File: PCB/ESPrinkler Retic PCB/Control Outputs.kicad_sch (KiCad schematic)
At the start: 108 parts, among them Q1 Q_NMOS, Q10 Q_NMOS, Q11 Q_NMOS, Q4 Q_NMOS, Q5 Q_NMOS, Q6 Q_NMOS, Q7 Q_NMOS, Q8 Q_NMOS, Q9 Q_NMOS, U1 MOC3063S, U10 MOC3063S, U3 MOC3063S, U4 MOC3063S, U5 MOC3063S, U6 MOC3063S, U7 MOC3063S, U8 MOC3063S, U9 MOC3063S

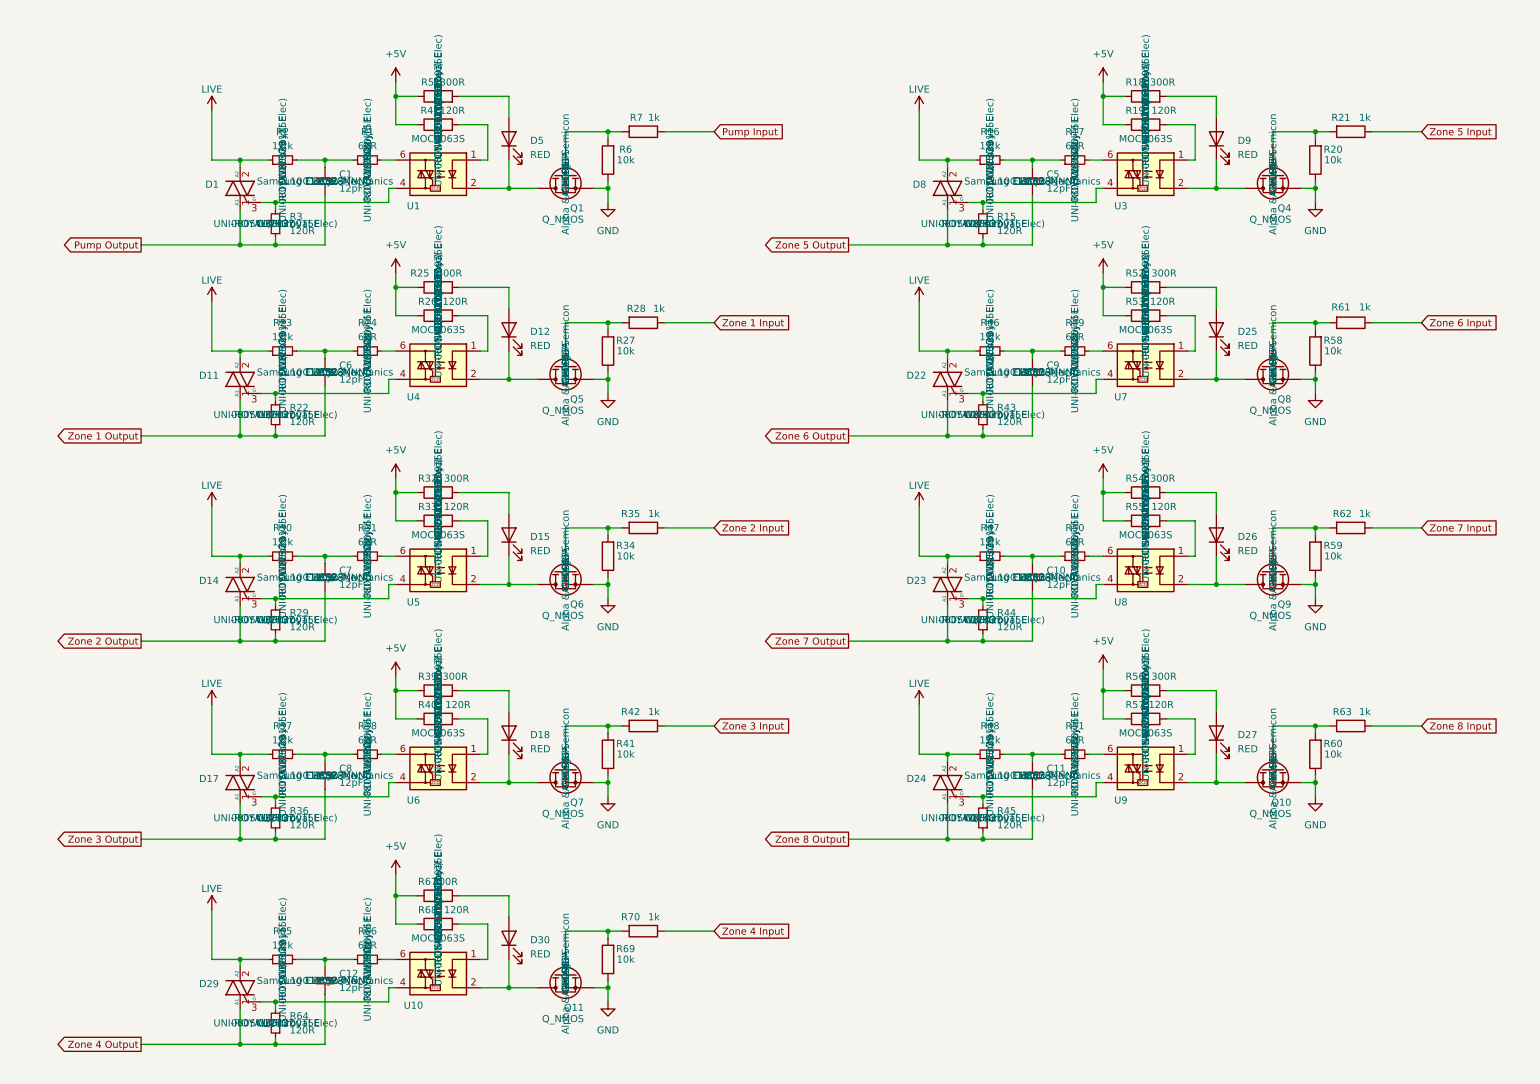
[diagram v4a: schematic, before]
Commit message: Initial schematic design completed
Finish initial schematic design and source all required components. DRC completed with only minor warnings (regarding net names, no worries). Move on to begin PCB design
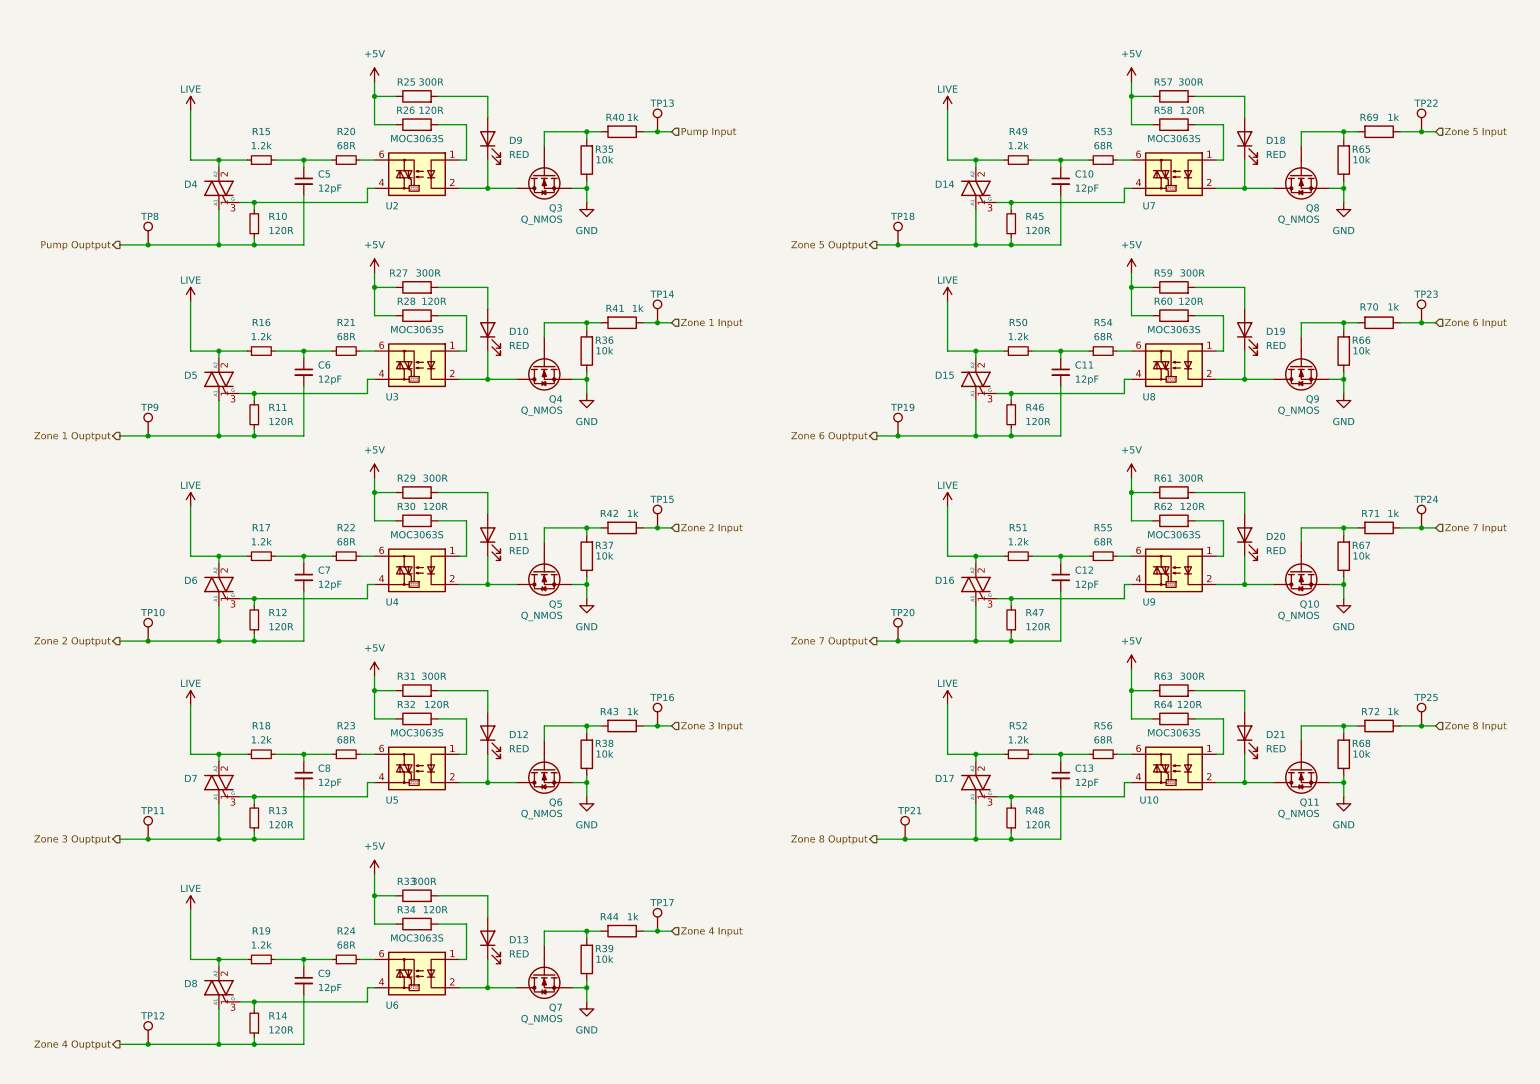
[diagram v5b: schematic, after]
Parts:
- added TP10, TP11, TP12, TP13, TP14, TP15, TP16, TP17, TP18, TP19, TP20, TP21, TP22, TP23, TP24, TP25, TP8, TP9: TestPoint, TestPoint:TestPoint_Pad_D1.5mm, symbol Connector:TestPoint
- D14: renamed from D8; footprint (none) -> Package_TO_SOT_THT:TO-220-3_Horizontal_TabDown; Manufacturer (none) -> STMicroelectronics; Manufacturer P/N (none) -> BTB16-600BWRG; Supplier (none) -> LCSC; Supplier P/N (none) -> C669873
- D15: renamed from D22; footprint (none) -> Package_TO_SOT_THT:TO-220-3_Horizontal_TabDown; Manufacturer (none) -> STMicroelectronics; Manufacturer P/N (none) -> BTB16-600BWRG; Supplier (none) -> LCSC; Supplier P/N (none) -> C669873
- D16: renamed from D23; footprint (none) -> Package_TO_SOT_THT:TO-220-3_Horizontal_TabDown; Manufacturer (none) -> STMicroelectronics; Manufacturer P/N (none) -> BTB16-600BWRG; Supplier (none) -> LCSC; Supplier P/N (none) -> C669873
- D17: renamed from D24; footprint (none) -> Package_TO_SOT_THT:TO-220-3_Horizontal_TabDown; Manufacturer (none) -> STMicroelectronics; Manufacturer P/N (none) -> BTB16-600BWRG; Supplier (none) -> LCSC; Supplier P/N (none) -> C669873
- D4: renamed from D1; footprint (none) -> Package_TO_SOT_THT:TO-220-3_Horizontal_TabDown; Manufacturer (none) -> STMicroelectronics; Manufacturer P/N (none) -> BTB16-600BWRG; Supplier (none) -> LCSC; Supplier P/N (none) -> C669873
- D5: renamed from D11; footprint (none) -> Package_TO_SOT_THT:TO-220-3_Horizontal_TabDown; Manufacturer (none) -> STMicroelectronics; Manufacturer P/N (none) -> BTB16-600BWRG; Supplier (none) -> LCSC; Supplier P/N (none) -> C669873
- D6: renamed from D14; footprint (none) -> Package_TO_SOT_THT:TO-220-3_Horizontal_TabDown; Manufacturer (none) -> STMicroelectronics; Manufacturer P/N (none) -> BTB16-600BWRG; Supplier (none) -> LCSC; Supplier P/N (none) -> C669873
- D7: renamed from D17; footprint (none) -> Package_TO_SOT_THT:TO-220-3_Horizontal_TabDown; Manufacturer (none) -> STMicroelectronics; Manufacturer P/N (none) -> BTB16-600BWRG; Supplier (none) -> LCSC; Supplier P/N (none) -> C669873
- D8: renamed from D29; footprint (none) -> Package_TO_SOT_THT:TO-220-3_Horizontal_TabDown; Manufacturer (none) -> STMicroelectronics; Manufacturer P/N (none) -> BTB16-600BWRG; Supplier (none) -> LCSC; Supplier P/N (none) -> C669873
- renumbered C5 to C10, C9 to C11, C10 to C12, C11 to C13, C1 to C5, C12 to C9, D12 to D10, D15 to D11, D18 to D12, D30 to D13, D9 to D18, D25 to D19, D26 to D20, D27 to D21, D5 to D9, Q9 to Q10, Q10 to Q11, Q1 to Q3, Q5 to Q4, Q6 to Q5, Q7 to Q6, Q11 to Q7, Q4 to Q8, Q8 to Q9, R3 to R10, R22 to R11, R29 to R12, R36 to R13, R64 to R14, R2 to R15, R23 to R16, R30 to R17, R37 to R18, R65 to R19, R1 to R20, R24 to R21, R31 to R22, R38 to R23, R66 to R24, R5 to R25, R4 to R26, R25 to R27, R26 to R28, R32 to R29, R33 to R30, R39 to R31, R40 to R32, R67 to R33, R68 to R34, R6 to R35, R27 to R36, R34 to R37, R41 to R38, R69 to R39, R7 to R40, R28 to R41, R35 to R42, R42 to R43, R70 to R44, R15 to R45, R43 to R46, R44 to R47, R45 to R48, R16 to R49, R46 to R50, R47 to R51, R48 to R52, R17 to R53, R49 to R54, R50 to R55, R51 to R56, R18 to R57, R19 to R58, R52 to R59, R53 to R60, R54 to R61, R55 to R62, R56 to R63, R57 to R64, R20 to R65, R58 to R66, R59 to R67, R60 to R68, R21 to R69, R61 to R70, R62 to R71, R63 to R72, U9 to U10, U1 to U2, U4 to U3, U5 to U4, U6 to U5, U10 to U6, U3 to U7, U7 to U8, U8 to U9
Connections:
- net Pump Input: now also TP13.1
- net Zone 1 Input: now also TP14.1
- net Zone 2 Input: now also TP15.1
- net Zone 3 Input: now also TP16.1
- net Zone 4 Input: now also TP17.1
- net Zone 5 Input: now also TP22.1
- net Zone 6 Input: now also TP23.1
- net Zone 7 Input: now also TP24.1
- net Zone 8 Input: now also TP25.1
- net Pump Output renamed Pump Ouptput
- net Pump Ouptput: now also TP8.1
- net Zone 1 Output renamed Zone 1 Ouptput
- net Zone 1 Ouptput: now also TP9.1
- net Zone 2 Output renamed Zone 2 Ouptput
- net Zone 2 Ouptput: now also TP10.1
- net Zone 3 Output renamed Zone 3 Ouptput
- net Zone 3 Ouptput: now also TP11.1
- net Zone 4 Output renamed Zone 4 Ouptput
- net Zone 4 Ouptput: now also TP12.1
- net Zone 5 Output renamed Zone 5 Ouptput
- net Zone 5 Ouptput: now also TP18.1
- net Zone 6 Output renamed Zone 6 Ouptput
- net Zone 6 Ouptput: now also TP19.1
- net Zone 7 Output renamed Zone 7 Ouptput
- net Zone 7 Ouptput: now also TP20.1
- net Zone 8 Output renamed Zone 8 Ouptput
- net Zone 8 Ouptput: now also TP21.1
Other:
- moved on the sheet: C10, C11, C12, C13, C5, C6, C7, C8, C9, D10, D11, D12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

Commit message: PCB and SCH work
Fix symbol issue for mosfet.

Continue PCB design layout
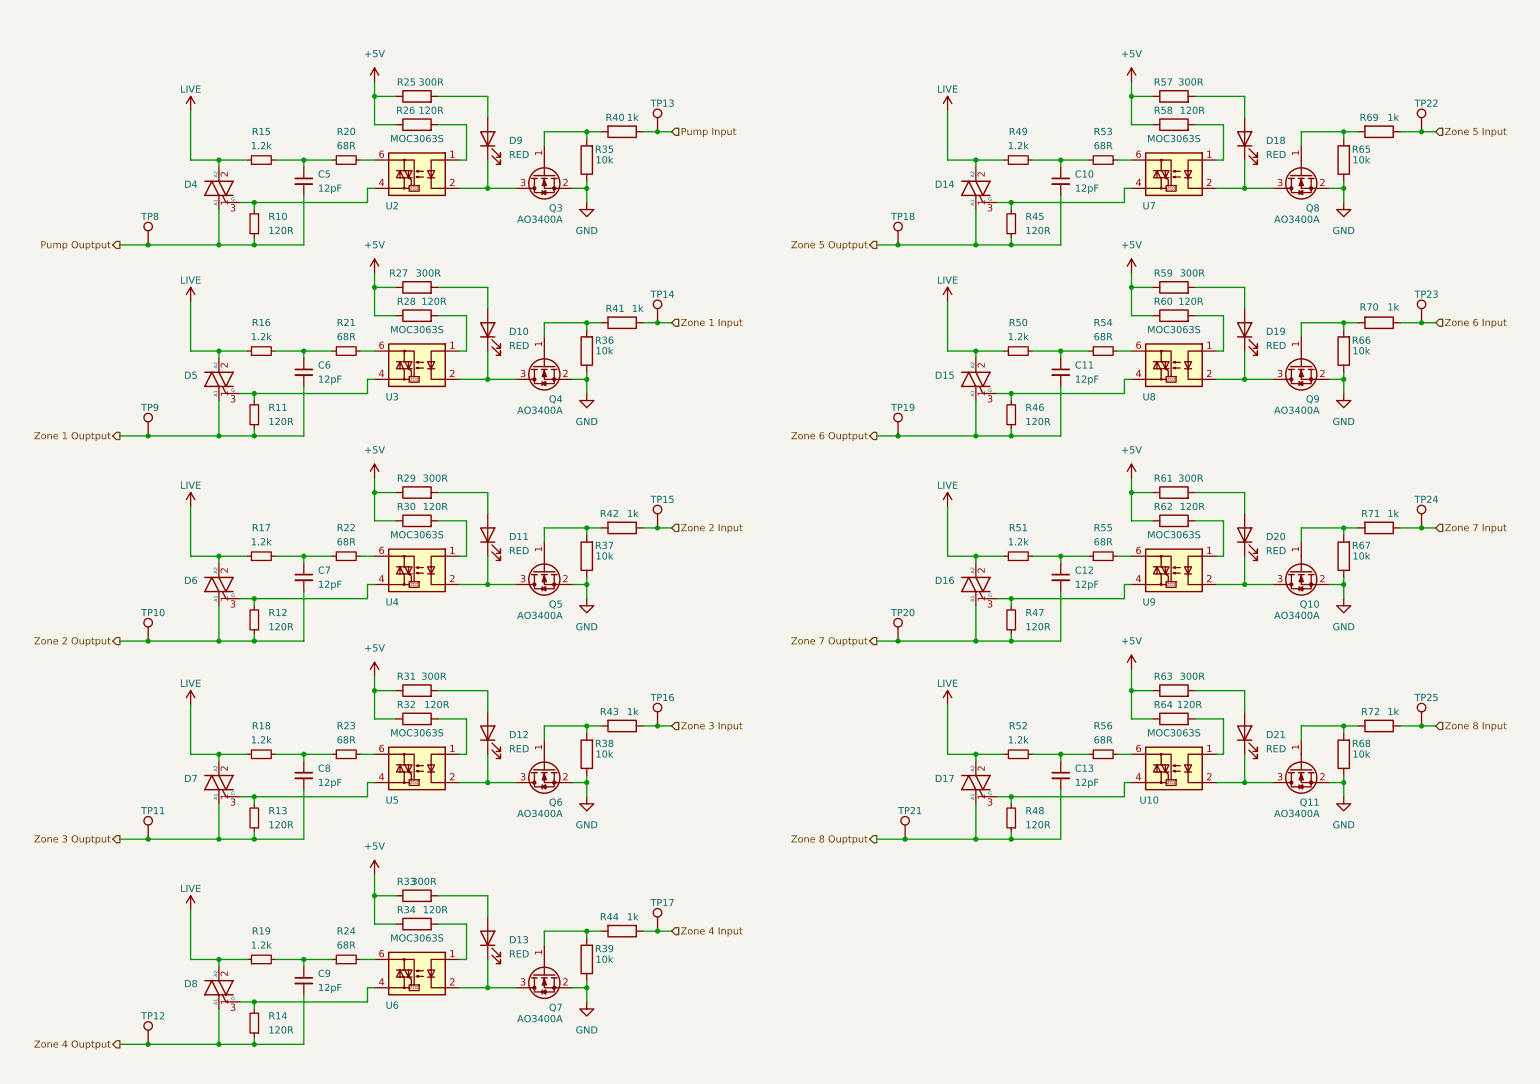
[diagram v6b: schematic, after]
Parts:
- Q10, Q11, Q3, Q4, Q5, Q6, Q7, Q8, Q9: value Q_NMOS -> AO3400A; symbol Device:Q_NMOS -> Transistor_FET:Q_NMOS_GSD
- U10, U2, U3, U4, U5, U6, U7, U8, U9: footprint Package_SO:SOP-8_6.605x9.655mm_P2.54mm -> Footprints:MOC306XS_LTO-M
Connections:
- net GND: now also Q10.2 (S), Q11.2 (S), Q3.2 (S), Q4.2 (S), Q5.2 (S), Q6.2 (S), Q7.2 (S), Q8.2 (S), Q9.2 (S); no longer Q10.S, Q11.S, Q3.S, Q4.S, Q5.S, Q6.S, Q7.S, Q8.S, Q9.S
- net at R38.2, R43.2: now also Q6.1 (G); no longer Q6.G
- net at R68.2, R72.2: now also Q11.1 (G); no longer Q11.G
- net at D19.1 (K), U8.2: now also Q9.3 (D); no longer Q9.D
- net at D13.1 (K), U6.2: now also Q7.3 (D); no longer Q7.D
- net at D12.1 (K), U5.2: now also Q6.3 (D); no longer Q6.D
- net at D11.1 (K), U4.2: now also Q5.3 (D); no longer Q5.D
- net at D9.1 (K), U2.2: now also Q3.3 (D); no longer Q3.D
- net at D18.1 (K), U7.2: now also Q8.3 (D); no longer Q8.D
- net at R65.2, R69.2: now also Q8.1 (G); no longer Q8.G
- net at R36.2, R41.2: now also Q4.1 (G); no longer Q4.G
- net at D21.1 (K), U10.2: now also Q11.3 (D); no longer Q11.D
- net at R37.2, R42.2: now also Q5.1 (G); no longer Q5.G
- net at R39.2, R44.2: now also Q7.1 (G); no longer Q7.G
- net at R35.2, R40.2: now also Q3.1 (G); no longer Q3.G
- net at R66.2, R70.2: now also Q9.1 (G); no longer Q9.G
- net at D20.1 (K), U9.2: now also Q10.3 (D); no longer Q10.D
- net at R67.2, R71.2: now also Q10.1 (G); no longer Q10.G
- net at D10.1 (K), U3.2: now also Q4.3 (D); no longer Q4.D
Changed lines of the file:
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@@
 			)
 		)
-		(property "Footprint" "Package_SO:SOP-8_6.605x9.655mm_P2.54mm"
+		(property "Footprint" "Footprints:MOC306XS_LTO-M"
 			(at 224.79 76.2 0)
 			(effects
@@
 			)
 		)
-		(property "Footprint" "Package_SO:SOP-8_6.605x9.655mm_P2.54mm"
+		(property "Footprint" "Footprints:MOC306XS_LTO-M"
 			(at 88.9 185.42 0)
 			(effects
@@
 			)
 		)
-		(property "Footprint" "Package_SO:SOP-8_6.605x9.655mm_P2.54mm"
+		(property "Footprint" "Footprints:MOC306XS_LTO-M"
 			(at 88.9 148.59 0)
 			(effects
@@
 			)
 		)
-		(property "Footprint" "Package_SO:SOP-8_6.605x9.655mm_P2.54mm"
+		(property "Footprint" "Footprints:MOC306XS_LTO-M"
 			(at 88.9 113.03 0)
 			(effects
@@
 			)
 		)
-		(property "Footprint" "Package_SO:SOP-8_6.605x9.655mm_P2.54mm"
+		(property "Footprint" "Footprints:MOC306XS_LTO-M"
 			(at 88.9 41.91 0)
 			(effects
@@
 	)
 	(symbol
-		(lib_id "Device:Q_NMOS")
+		(lib_id "Transistor_FET:Q_NMOS_GSD")
 		(at 242.57 36.83 90)
 		(mirror x)
@@
 			)
 		)
-		(property "Value" "Q_NMOS"
+		(property "Value" "AO3400A"
 			(at 245.872 44.958 90)
 			(effects
@@
 			)
 		)
-		(pin "D"
+		(pin "1"
 		)
-		(pin "S"
+		(pin "2"
 		)
-		(pin "G"
+		(pin "3"
 		)
 		(instances
@@
 	)
 	(symbol
-		(lib_id "Device:Q_NMOS")
+		(lib_id "Transistor_FET:Q_NMOS_GSD")
 		(at 242.57 143.51 90)
 		(mirror x)
@@
 			)
 		)
-		(property "Value" "Q_NMOS"
+		(property "Value" "AO3400A"
 			(at 245.872 151.638 90)
 			(effects
@@
 			)
 		)
-		(pin "D"
+		(pin "3"
 		)
-		(pin "S"
+		(pin "2"
 		)
-		(pin "G"
+		(pin "1"
 		)
 		(instances
@@
 	)
 	(symbol
-		(lib_id "Device:Q_NMOS")
+		(lib_id "Transistor_FET:Q_NMOS_GSD")
 		(at 242.57 71.12 90)
 		(mirror x)
@@
 			)
 		)
-		(property "Value" "Q_NMOS"
+		(property "Value" "AO3400A"
 			(at 245.872 79.248 90)
 			(effects
@@
 			)
 		)
-		(pin "D"
+		(pin "2"
 		)
-		(pin "S"
+		(pin "3"
 		)
-		(pin "G"
+		(pin "1"
 		)
 		(instances
@@
 	)
 	(symbol
-		(lib_id "Device:Q_NMOS")
+		(lib_id "Transistor_FET:Q_NMOS_GSD")
 		(at 106.68 36.83 90)
 		(mirror x)
@@
 			)
 		)
-		(property "Value" "Q_NMOS"
+		(property "Value" "AO3400A"
 			(at 109.982 44.958 90)
 			(effects
@@
 			)
 		)
-		(pin "D"
+		(pin "3"
 		)
-		(pin "S"
+		(pin "1"
 		)
-		(pin "G"
+		(pin "2"
 		)
 		(instances
@@
 	)
 	(symbol
-		(lib_id "Device:Q_NMOS")
+		(lib_id "Transistor_FET:Q_NMOS_GSD")
 		(at 106.68 71.12 90)
 		(mirror x)
@@
 			)
 		)
-		(property "Value" "Q_NMOS"
+		(property "Value" "AO3400A"
 			(at 109.982 79.248 90)
 			(effects
@@
 			)
 		)
-		(pin "D"
+		(pin "2"
 		)
-		(pin "S"
+		(pin "3"
 		)
-		(pin "G"
+		(pin "1"
 		)
 		(instances
@@
 			)
 		)
-		(property "Footprint" "Package_SO:SOP-8_6.605x9.655mm_P2.54mm"
+		(property "Footprint" "Footprints:MOC306XS_LTO-M"
 			(at 224.79 113.03 0)
 			(effects
@@
 	)
 	(symbol
-		(lib_id "Device:Q_NMOS")
+		(lib_id "Transistor_FET:Q_NMOS_GSD")
 		(at 242.57 107.95 90)
 		(mirror x)
@@
 			)
 		)
-		(property "Value" "Q_NMOS"
+		(property "Value" "AO3400A"
 			(at 245.872 116.078 90)
 			(effects
@@
 			)
 		)
-		(pin "D"
+		(pin "3"
 		)
-		(pin "S"
+		(pin "1"
 		)
-		(pin "G"
+		(pin "2"
 		)
 		(instances
@@
 	)
 	(symbol
-		(lib_id "Device:Q_NMOS")
+		(lib_id "Transistor_FET:Q_NMOS_GSD")
 		(at 106.68 143.51 90)
 		(mirror x)
@@
 			)
 		)
-		(property "Value" "Q_NMOS"
+		(property "Value" "AO3400A"
 			(at 109.982 151.638 90)
 			(effects
@@
 			)
 		)
-		(pin "D"
+		(pin "1"
 		)
-		(pin "S"
+		(pin "3"
 		)
-		(pin "G"
+		(pin "2"
 		)
 		(instances
@@
 			)
 		)
-		(property "Footprint" "Package_SO:SOP-8_6.605x9.655mm_P2.54mm"
+		(property "Footprint" "Footprints:MOC306XS_LTO-M"
 			(at 224.79 41.91 0)
 			(effects
@@
 			)
 		)
-		(property "Footprint" "Package_SO:SOP-8_6.605x9.655mm_P2.54mm"
+		(property "Footprint" "Footprints:MOC306XS_LTO-M"
 			(at 88.9 76.2 0)
 			(effects
@@
 	)
 	(symbol
-		(lib_id "Device:Q_NMOS")
+		(lib_id "Transistor_FET:Q_NMOS_GSD")
 		(at 106.68 107.95 90)
 		(mirror x)
@@
 			)
 		)
-		(property "Value" "Q_NMOS"
+		(property "Value" "AO3400A"
 			(at 109.982 116.078 90)
 			(effects
@@
 			)
 		)
-		(pin "D"
+		(pin "1"
 		)
-		(pin "S"
+		(pin "3"
 		)
-		(pin "G"
+		(pin "2"
 		)
 		(instances
@@
 	)
 	(symbol
-		(lib_id "Device:Q_NMOS")
+		(lib_id "Transistor_FET:Q_NMOS_GSD")
 		(at 106.68 180.34 90)
 		(mirror x)
@@
 			)
 		)
-		(property "Value" "Q_NMOS"
+		(property "Value" "AO3400A"
 			(at 109.982 188.468 90)
 			(effects
@@
 			)
 		)
-		(pin "D"
+		(pin "2"
 		)
-		(pin "S"
+		(pin "1"
 		)
-		(pin "G"
+		(pin "3"
 		)
 		(instances
@@
 			)
 		)
-		(property "Footprint" "Package_SO:SOP-8_6.605x9.655mm_P2.54mm"
+		(property "Footprint" "Footprints:MOC306XS_LTO-M"
 			(at 224.79 148.59 0)
 			(effects
